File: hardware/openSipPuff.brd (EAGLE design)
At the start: 30.2 x 58.4 mm, 26 parts, among them J1 AVR_SPI_PRG_62X3_LOCK, J2 I2C, U1 ATMEGA32U4TQFP, U2 AD8223, U3 MPX12GP, Y1 16MHz

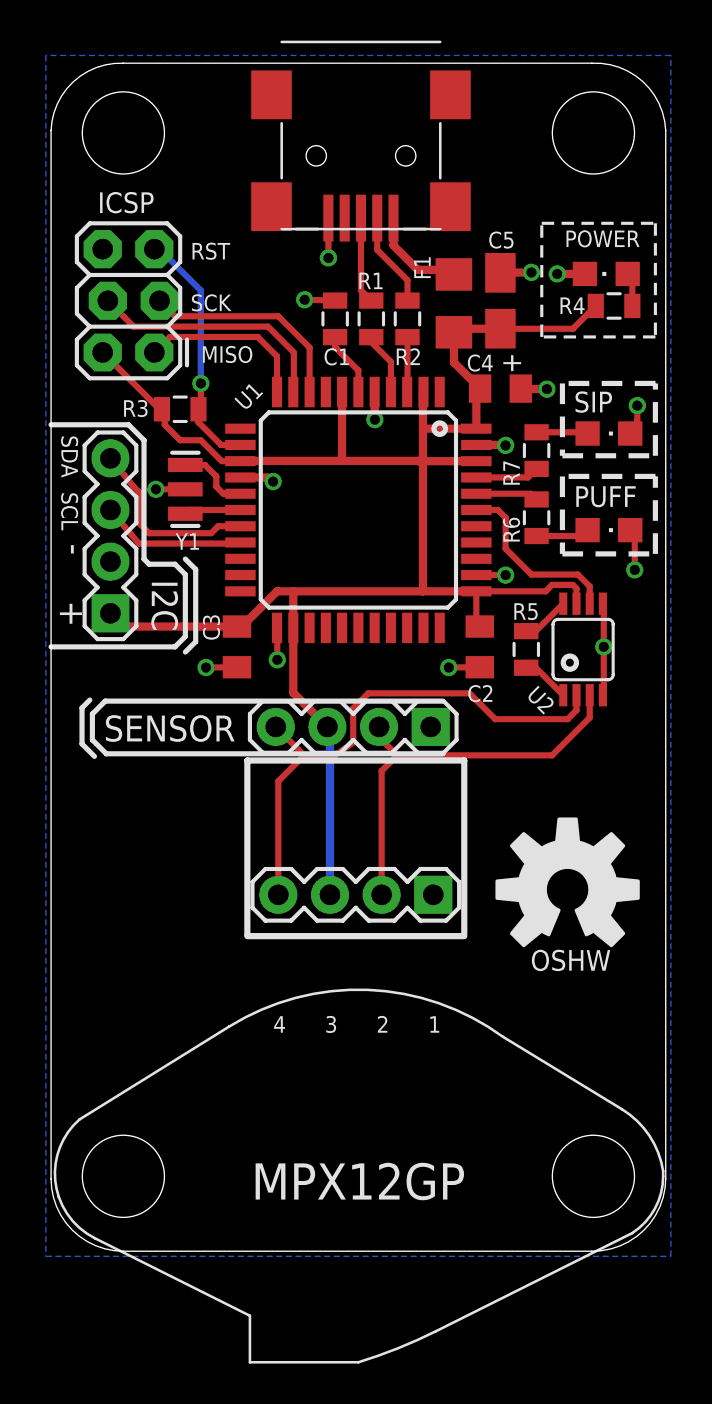
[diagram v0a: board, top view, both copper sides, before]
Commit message: Major board updates with new sensor, I2C interface, and more
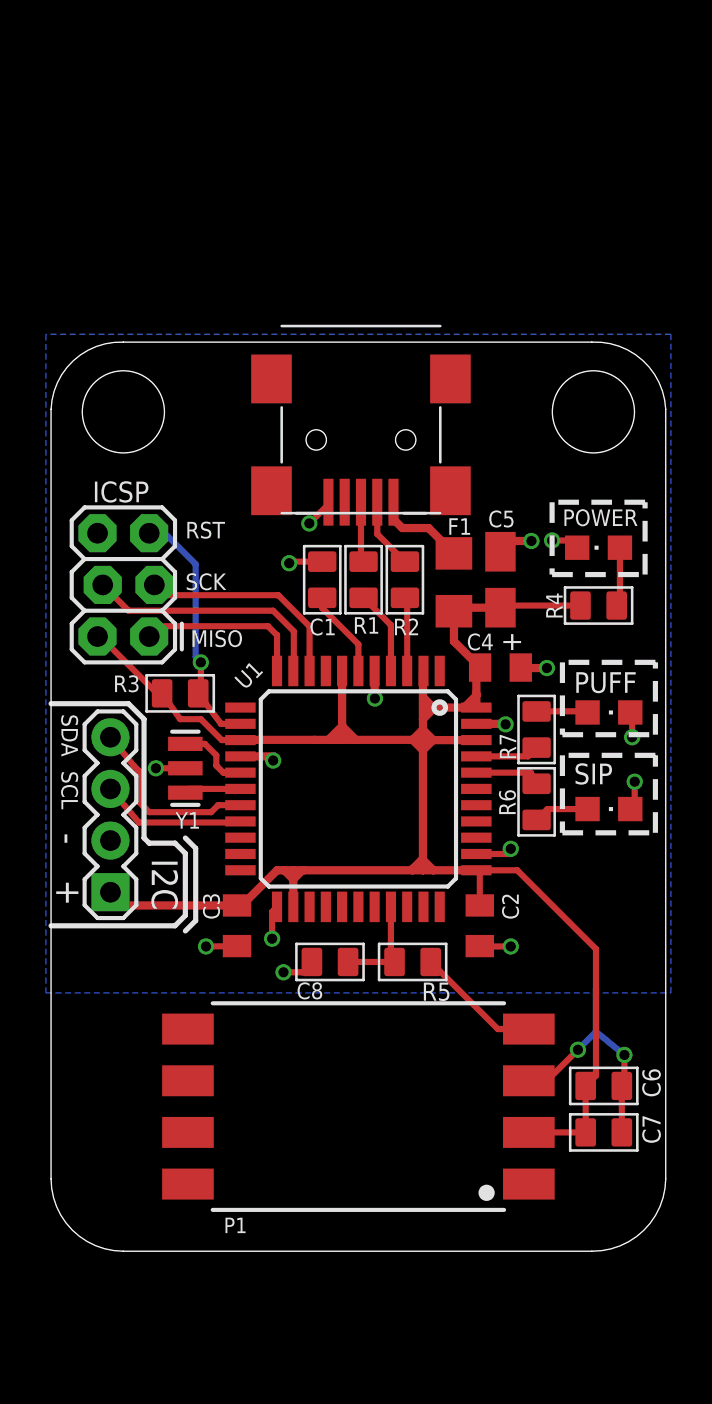
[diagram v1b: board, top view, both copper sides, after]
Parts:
- removed LOGO1: OSHW-LOGOL, SparkFun-Aesthetics:OSHW-LOGO-L
- removed SENSOR, SENSOR1: (no value), SparkFun-Connectors:1X04
- removed U2: AD8223, sip-and-puff:MSOP-8
- removed U3: MPX12GP, sip-and-puff:MPX12GP
- added C6: 1uf, Seeed-Capacitor:C0805
- added C7: 0.01uF, Seeed-Capacitor:C0805
- added C8: 0.33uF, Seeed-Capacitor:C0805
- added P1: MPXV7007GP, MPXV7007GP:SOP8
- C1: value 1uF -> 1uf; device SparkFun-Capacitors:0805 -> Seeed-Capacitor:C0805
- R1, R2: device SparkFun-Resistors:0805 -> Seeed-OPL-Resistor:R0805
- R3: value 10k -> 10K; device SparkFun-Resistors:0805 -> Seeed-Resistor:R0805
- R4, R6, R7: device SparkFun-Resistors:0805 -> Seeed-Resistor:R0805
- R5: value 1.3k -> 750; device SparkFun-Resistors:0805 -> Seeed-Resistor:R0805
- moved R5 16.4 mm to (17.8, 14.2)
- moved R4 14.8 mm to (26.9, 31.8), turned to 270 degrees
- moved J1 14.0 mm to (4.83, 30.2)
- moved R3 14.0 mm to (6.35, 27.4), turned to 270 degrees
- moved CN2 14.0 mm to (15.2, 40.9)
- moved R6 14.0 mm to (23.9, 22.1), turned to 0 degrees
- moved Y1 13.7 mm to (6.60, 23.7)
- moved C2 13.7 mm to (21.1, 16.0)
- moved C3 13.7 mm to (9.14, 16.0)
- moved F1 13.7 mm to (19.8, 32.9)
- moved J2 13.7 mm to (2.92, 17.7)
- moved C4 13.7 mm to (22.1, 28.7)
- moved LED2 13.7 mm to (27.4, 21.7)
- moved LED3 13.7 mm to (27.4, 26.5)
- moved R7 13.7 mm to (23.9, 25.7), turned to 180 degrees
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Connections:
- removed net N$11: R5.1, U2.8
- removed net N$13: SENSOR.4, SENSOR1.4, U2.2
- removed net OUTPUT: U1.39, U2.6
- net 5V: now also C6.2, C7.2, P1.2; no longer SENSOR.3, SENSOR1.3, U2.7
- net GND: now also C6.1, C7.1, C8.1, P1.3; no longer SENSOR.1, SENSOR1.1, U2.4, U2.5
- net N$10: now also P1.4, R5.1; no longer SENSOR.2, SENSOR1.2, U2.3
- net N$7: now also C8.2, U1.30; no longer U2.1
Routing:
- net N$13: track 26.4 -> 0.00 mm
- net N$10: track 20.3 -> 6.19 mm
- net GND: track 27.9 -> 37.5 mm, vias 16 -> 18
- net OUTPUT: track 8.88 -> 0.00 mm
- net 5V: track 92.5 -> 100.5 mm
- net N$7: track 2.38 -> 5.07 mm
- net N$11: track 2.38 -> 0.00 mm
- net N$12: track 1.67 -> 2.91 mm
- net D-: track 4.67 -> 3.48 mm
- net N$3: track 3.17 -> 4.33 mm
- net N$1: track 3.10 -> 4.16 mm
- net D+: track 4.26 -> 3.21 mm
- net N$2: track 2.70 -> 3.65 mm
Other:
- board size 30.2 x 58.4 mm -> 30.2 x 44.7 mm
- board text removed: "Designed by Jason Webb"
- board text removed: "OSHW"
- board text removed: "http://jason-webb.info"
- board text removed: "openSip+Puff"
- board text removed: "rev C"

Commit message: Updating MPXV7007GP footprint to include hole for underside port
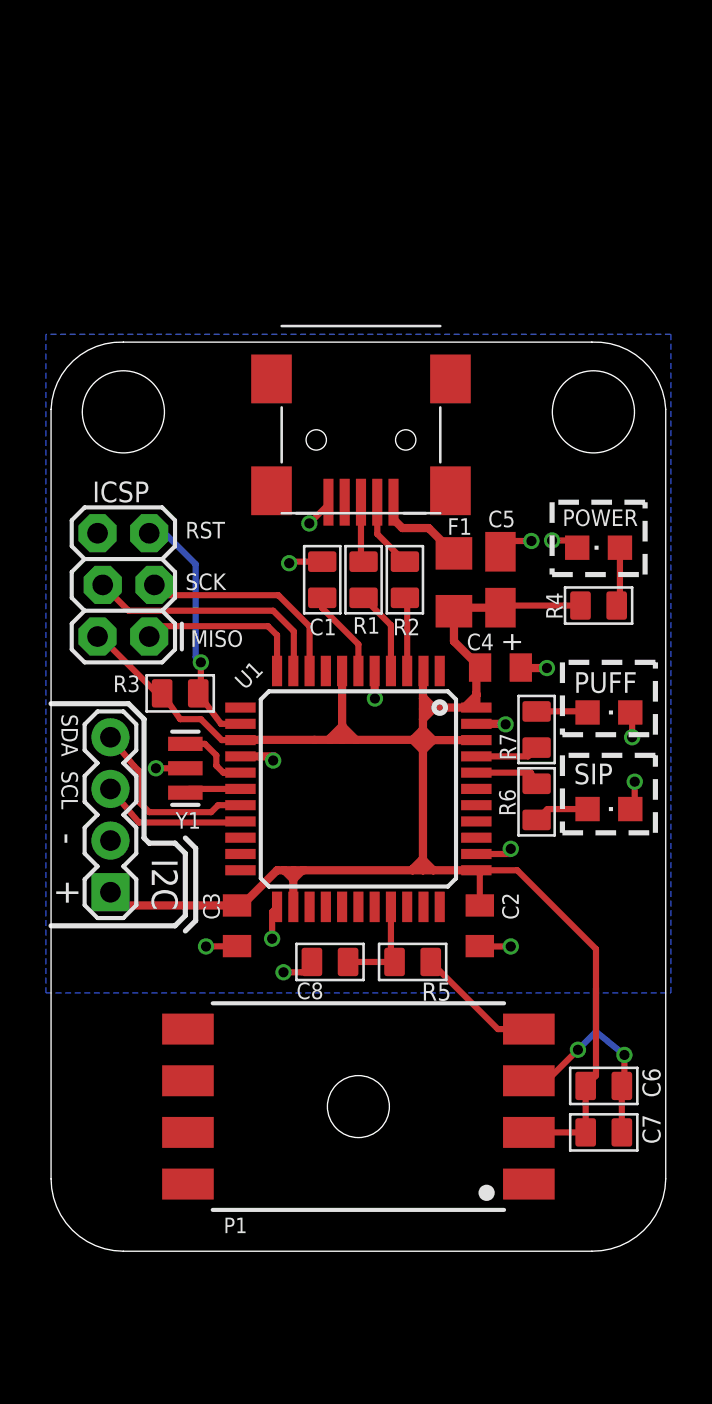
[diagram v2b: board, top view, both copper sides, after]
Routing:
- net GND: track 37.5 -> 36.7 mm
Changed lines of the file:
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@@
 <wire x1="12.7" y1="35.7886" x2="13.64" y2="36.7286" width="0.3048" layer="1"/>
 <wire x1="13.64" y1="36.7286" x2="13.64" y2="36.83" width="0.3048" layer="1"/>
-<wire x1="22.098" y1="34.395" x2="22.613440625" y2="34.910440625" width="0.4064" layer="1"/>
 <wire x1="13.335" y1="33.909" x2="11.7856" y2="33.909" width="0.3048" layer="1"/>
 <wire x1="11.7856" y1="33.909" x2="11.7094" y2="33.8328" width="0.3048" layer="1"/>
@@
 <wire x1="28.575" y1="26.3992" x2="28.482" y2="26.4922" width="0.3048" layer="1"/>
 <wire x1="28.702" y1="21.9624" x2="28.482" y2="21.7424" width="0.3048" layer="1"/>
-<wire x1="22.098" y1="34.395" x2="22.628" y2="34.925" width="0.4064" layer="1"/>
-<wire x1="22.628" y1="34.925" x2="23.622" y2="34.925" width="0.4064" layer="1"/>
 <wire x1="25.874" y1="34.5948" x2="25.5184" y2="34.9504" width="0.3048" layer="1"/>
 <wire x1="25.5184" y1="34.9504" x2="24.638" y2="34.9504" width="0.3048" layer="1"/>
+<wire x1="22.098" y1="34.395" x2="22.628" y2="34.925" width="0.3048" layer="1"/>
+<wire x1="22.628" y1="34.925" x2="23.622" y2="34.925" width="0.3048" layer="1"/>
 </signal>
 <signal name="N$3">
